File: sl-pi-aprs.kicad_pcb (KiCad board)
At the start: 2 copper layers, 65.2 x 30.2 mm, 33 parts, among them J1 Power, J10 PTT Disable, J2 RPi Header, J3 Radio, J4 Radio In, J5 Audio In, J6 Audio In, J7 Audio Out, J8 Audio Out, J9 GPS Header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

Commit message: reorder LEDs.  Labelling
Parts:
- moved D1 7.65 mm to (107.8, 89.8)
- moved R8 7.65 mm to (107.8, 89.8)
- moved D4 7.65 mm to (107.8, 97.4)
- moved R7 7.65 mm to (107.8, 97.4)
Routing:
- net Net-(D4-Pad1): track 5.07 -> 12.0 mm
- net +3V3: track 68.7 -> 73.8 mm
- net Net-(D1-Pad2): track 0.00 -> 2.97 mm, vias 0 -> 1
- net Net-(D3-Pad2): track 0.00 -> 2.96 mm, vias 0 -> 1
- net Net-(D2-Pad2): track 0.00 -> 2.96 mm, vias 0 -> 1
- net Net-(D4-Pad2): track 0.00 -> 2.96 mm, vias 0 -> 1
- net +5V: track 21.8 -> 20.1 mm
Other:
- board text added: "SPK"
- board text removed: "AF"
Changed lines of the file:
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@@
     (thickness 1.6)
     (drawings 25)
-    (tracks 120)
+    (tracks 139)
     (zones 0)
     (modules 33)
@@
   )
   (module Resistor_SMD:R_0603_1608Metric_Pad0.98x0.95mm_HandSolder (layer B.Cu)
-    (at 107.8 97.415)
+    (at 107.8 89.765)
     (descr "Resistor SMD 0603 (1608 Metric), square (rectangular) end terminal, IPC_7351 nominal with elongated pad for handsoldering. (Body size source: IPC-SM-782 page 72, https://www.pcb-3d.com/wordpress/wp-content/uploads/ipc-sm-782a_amendment_1_and_2.pdf), generated with kicad-footprint-generator")
     (tags "resistor handsolder")
@@
   )
   (module Resistor_SMD:R_0603_1608Metric_Pad0.98x0.95mm_HandSolder (layer B.Cu)
-    (at 107.8 89.795)
+    (at 107.7998 97.443)
     (descr "Resistor SMD 0603 (1608 Metric), square (rectangular) end terminal, IPC_7351 nominal with elongated pad for handsoldering. (Body size source: IPC-SM-782 page 72, https://www.pcb-3d.com/wordpress/wp-content/uploads/ipc-sm-782a_amendment_1_and_2.pdf), generated with kicad-footprint-generator")
     (tags "resistor handsolder")
@@
   )
   (module LED_SMD:LED_1206_3216Metric (layer F.Cu)
-    (at 107.8 97.415 180)
+    (at 107.8 89.765 180)
     (descr "LED SMD 1206 (3216 Metric), square (rectangular) end terminal, IPC_7351 nominal, (Body size source: http://www.tortai-tech.com/upload/download/2011102023233369053.pdf), generated with kicad-footprint-generator")
     (tags LED)
@@
   )
   (module LED_SMD:LED_1206_3216Metric (layer F.Cu)
-    (at 107.8 89.795 180)
+    (at 107.7998 97.443 180)
     (descr "LED SMD 1206 (3216 Metric), square (rectangular) end terminal, IPC_7351 nominal, (Body size source: http://www.tortai-tech.com/upload/download/2011102023233369053.pdf), generated with kicad-footprint-generator")
     (tags LED)
@@
     (effects (font (size 0.75 0.75) (thickness 0.1875)))
   )
-  (gr_text "GPS\n" (at 110.75 89.85 270) (layer F.SilkS)
+  (gr_text "GPS\n" (at 110.7498 97.498 270) (layer F.SilkS)
     (effects (font (size 0.75 0.75) (thickness 0.1875)))
   )
@@
     (effects (font (size 0.75 0.75) (thickness 0.1875)))
   )
-  (gr_text PWR (at 110.75 97.4 270) (layer F.SilkS)
+  (gr_text PWR (at 110.75 89.75 270) (layer F.SilkS)
     (effects (font (size 0.75 0.75) (thickness 0.1875)))
   )
@@
     (effects (font (size 1.5 1.5) (thickness 0.3)))
   )
-  (gr_text AF (at 124.2605 104.2305) (layer F.SilkS)
+  (gr_text SPK (at 125.2474 104.2162) (layer F.SilkS)
     (effects (font (size 1.5 1.5) (thickness 0.3)))
   )
@@
   (segment (start 121.89 98.085) (end 115.5 104.475) (width 0.25) (layer B.Cu) (net 2))
   (segment (start 121.89 96.835) (end 121.89 98.085) (width 0.25) (layer B.Cu) (net 2))
-  (segment (start 110.617501 95.509999) (end 108.7125 97.415) (width 0.25) (layer B.Cu) (net 3))
-  (segment (start 115.914999 95.509999) (end 110.617501 95.509999) (width 0.25) (layer B.Cu) (net 3))
-  (segment (start 115.99 95.585) (end 115.914999 95.509999) (width 0.25) (layer B.Cu) (net 3))
-  (segment (start 115.99 96.835) (end 115.99 95.585) (width 0.25) (layer B.Cu) (net 3))
   (segment (start 116 96.845) (end 115.99 96.835) (width 0.25) (layer B.Cu) (net 3))
   (segment (start 116 99.2375) (end 116 96.845) (width 0.25) (layer B.Cu) (net 3))
@@
   (segment (start 115.99 90.535) (end 115.99 87.61) (width 0.25) (layer B.Cu) (net 3))
   (segment (start 115.54 83.81) (end 113 83.81) (width 0.25) (layer B.Cu) (net 3))
+  (segment (start 115.22 89.765) (end 115.99 90.535) (width 0.25) (layer B.Cu) (net 3))
+  (segment (start 108.7125 89.765) (end 115.22 89.765) (width 0.25) (layer B.Cu) (net 3))
   (segment (start 124.25 96.895) (end 124.19 96.835) (width 0.25) (layer B.Cu) (net 4))
   (segment (start 124.25 99.2375) (end 124.25 96.895) (width 0.25) (layer B.Cu) (net 4))
@@
   (segment (start 163.87499 98.72499) (end 124.76251 98.72499) (width 0.25) (layer B.Cu) (net 4))
   (segment (start 166.67 101.52) (end 163.87499 98.72499) (width 0.25) (layer B.Cu) (net 4))
+  (segment (start 108.7123 92.3352) (end 108.7125 92.335) (width 0.25) (layer B.Cu) (net 4))
+  (segment (start 108.7123 97.443) (end 108.7123 92.3352) (width 0.25) (layer B.Cu) (net 4))
+  (segment (start 106.4 89.765) (end 105.1574 89.765) (width 0.25) (layer F.Cu) (net 5))
+  (segment (start 105.1574 89.765) (end 105.1574 89.765) (width 0.25) (layer F.Cu) (net 5))
+  (via (at 105.1574 89.765) (size 0.8) (drill 0.4) (layers F.Cu B.Cu) (net 5))
+  (segment (start 106.8875 89.765) (end 105.1574 89.765) (width 0.25) (layer B.Cu) (net 5))
+  (segment (start 106.4 94.875) (end 105.162 94.875) (width 0.25) (layer F.Cu) (net 6))
+  (segment (start 105.162 94.875) (end 105.162 94.875) (width 0.25) (layer F.Cu) (net 6))
+  (via (at 105.162 94.875) (size 0.8) (drill 0.4) (layers F.Cu B.Cu) (net 6))
+  (segment (start 106.8875 94.875) (end 105.162 94.875) (width 0.25) (layer B.Cu) (net 6))
   (segment (start 111.010001 96.685001) (end 109.2 94.875) (width 0.25) (layer F.Cu) (net 7))
   (segment (start 115.705012 98.48501) (end 113.905003 96.685001) (width 0.25) (layer F.Cu) (net 7))
@@
   (segment (start 113.905003 96.685001) (end 111.010001 96.685001) (width 0.25) (layer F.Cu) (net 7))
   (segment (start 119.5 97.9) (end 118.91499 98.48501) (width 0.25) (layer F.Cu) (net 7))
+  (segment (start 106.4 92.335) (end 105.162 92.335) (width 0.25) (layer F.Cu) (net 8))
+  (segment (start 105.162 92.335) (end 105.162 92.335) (width 0.25) (layer F.Cu) (net 8))
+  (via (at 105.162 92.335) (size 0.8) (drill 0.4) (layers F.Cu B.Cu) (net 8))
+  (segment (start 106.8875 92.335) (end 105.162 92.335) (width 0.25) (layer B.Cu) (net 8))
   (segment (start 109.490001 92.625001) (end 109.2 92.335) (width 0.25) (layer F.Cu) (net 9))
   (segment (start 118.524999 92.625001) (end 109.490001 92.625001) (width 0.25) (layer F.Cu) (net 9))
@@
   (segment (start 132.070255 97.239745) (end 128.252245 97.239745) (width 0.25) (layer F.Cu) (net 23))
   (segment (start 133.21 96.1) (end 132.070255 97.239745) (width 0.25) (layer F.Cu) (net 23))
-  (segment (start 111.055 91.65) (end 109.2 89.795) (width 0.25) (layer F.Cu) (net 50))
-  (segment (start 113.5 91.65) (end 111.055 91.65) (width 0.25) (layer F.Cu) (net 50))
+  (segment (start 106.3998 97.443) (end 105.1646 97.443) (width 0.25) (layer F.Cu) (net 49))
+  (segment (start 105.1646 97.443) (end 105.1646 97.443) (width 0.25) (layer F.Cu) (net 49))
+  (via (at 105.1646 97.443) (size 0.8) (drill 0.4) (layers F.Cu B.Cu) (net 49))
+  (segment (start 106.8873 97.443) (end 105.1646 97.443) (width 0.25) (layer B.Cu) (net 49))
+  (segment (start 112.98499 91.13499) (end 113.5 91.65) (width 0.25) (layer F.Cu) (net 50))
+  (segment (start 108.58682 91.13499) (end 112.98499 91.13499) (width 0.25) (layer F.Cu) (net 50))
+  (segment (start 108.24999 91.47182) (end 108.58682 91.13499) (width 0.25) (layer F.Cu) (net 50))
+  (segment (start 108.24999 96.49319) (end 108.24999 91.47182) (width 0.25) (layer F.Cu) (net 50))
+  (segment (start 109.1998 97.443) (end 108.24999 96.49319) (width 0.25) (layer F.Cu) (net 50))
 )

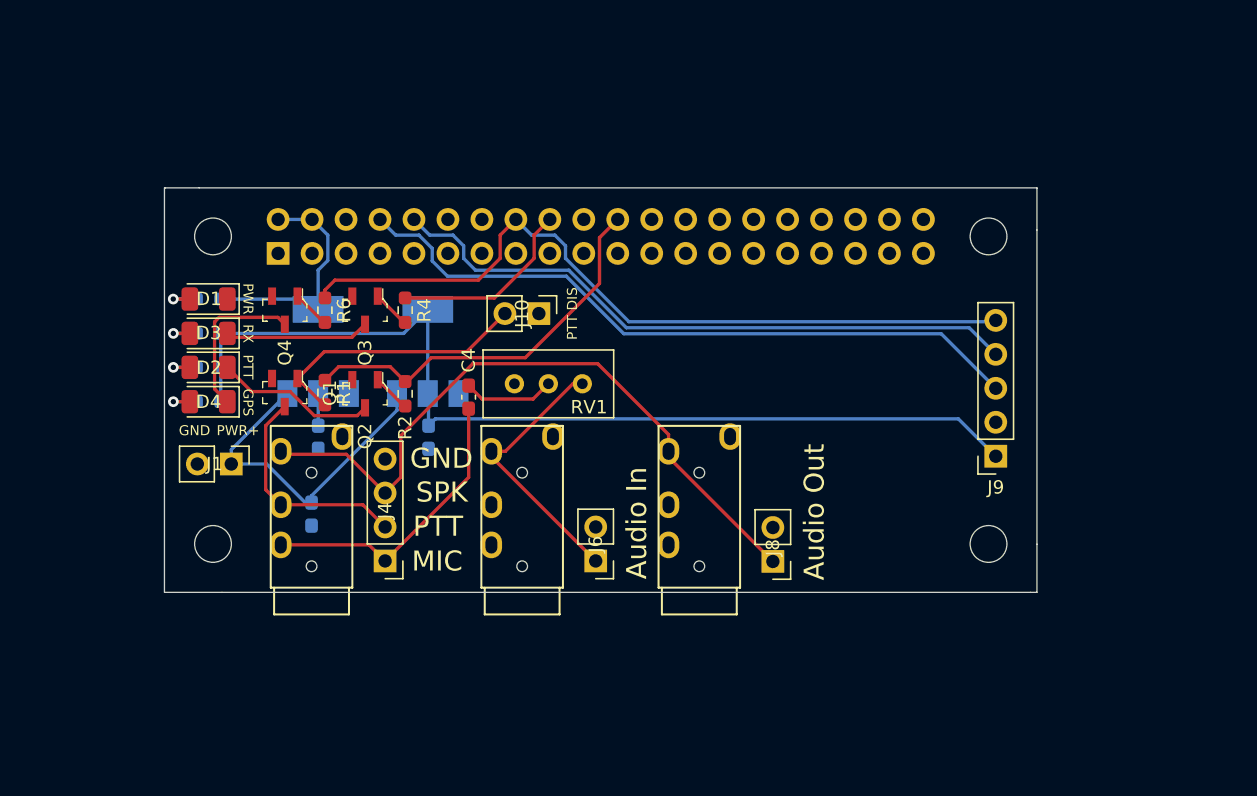
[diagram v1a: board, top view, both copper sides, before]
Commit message: Add ground planes and minor adjustments
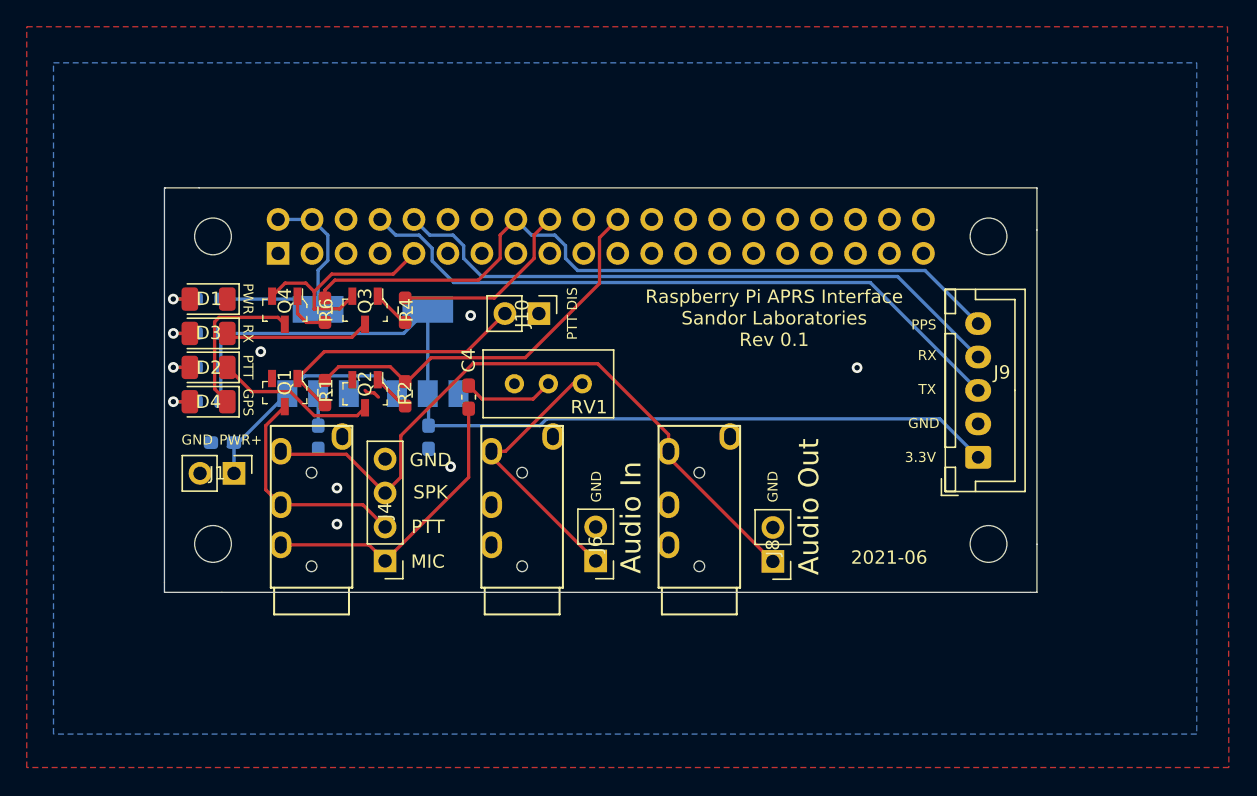
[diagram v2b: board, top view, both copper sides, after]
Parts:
- J9: footprint sl-pi-aprs:PinHeader_1x05_P2.54mm_Vertical_gt-u7_breakout -> Connector_JST:JST_XH_B5B-XH-A_1x05_P2.50mm_Vertical
- moved C1 8.54 mm to (108.8, 100.5), turned to 180 degrees
- moved J9 2.97 mm to (165.4, 101.6), turned to 90 degrees
- moved J1 0.73 mm to (109.7, 102.8)
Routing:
- net GND: track 0.00 -> 17.0 mm, vias 0 -> 6
- net +BATT: track 25.0 -> 17.6 mm
- net gps_pps: track 57.7 -> 56.4 mm
- net +3V3: track 73.8 -> 72.6 mm
- net pi_tx: track 51.8 -> 50.6 mm
- net pi_rx: track 48.2 -> 47.0 mm
- net (no net): track 0.00 -> 1.21 mm
- net Net-(Q4-Pad1): track 2.86 -> 3.71 mm
- added copper zone on B.Cu, net GND
- added copper zone on F.Cu, net GND
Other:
- board text added: "2021-06"
- board text added: "3.3V"
- board text added: "PPS"
- board text added: "Raspberry Pi APRS Interface Sandor Laboratories Rev 0.1"
- board text added: "TX"

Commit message: Final tweaks for REV 0.1
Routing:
- net GND: track 17.0 -> 143.5 mm, vias 6 -> 5
- net +5V: track 20.1 -> 21.8 mm
- net (no net): track 1.21 -> 0.00 mm
- net +3V3: track 72.6 -> 73.5 mm
- net gps_pps: track 56.4 -> 56.9 mm
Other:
- net class Power added: clearance 0.2, trace_width 0.5, via_dia 0.8, via_drill 0.4
- net class Power Rail added: clearance 0.2, trace_width 0.75, via_dia 0.8, via_drill 0.4
- board text added: "MIC Gain"
- board text added: "PTT Diasble"
- board text removed: "PTT DIS"
